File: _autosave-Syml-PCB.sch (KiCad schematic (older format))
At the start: 13 parts

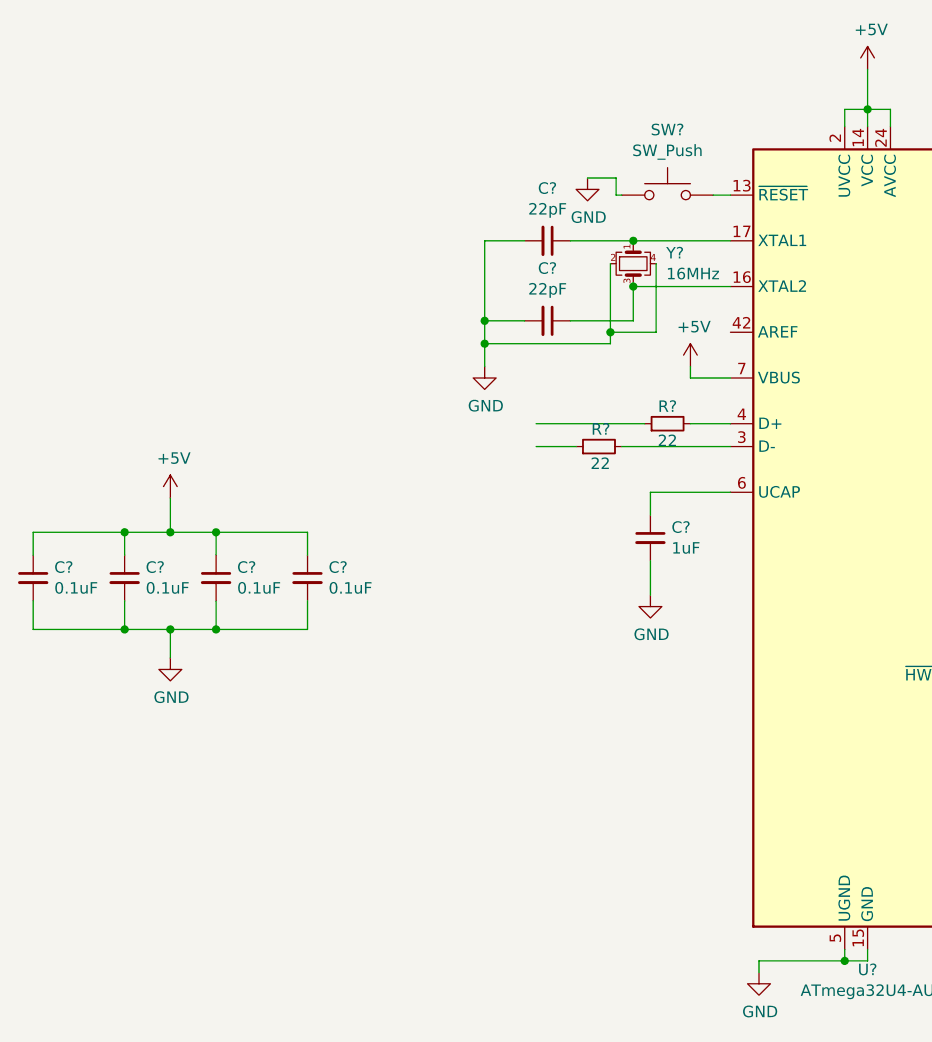
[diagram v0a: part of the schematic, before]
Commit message: Add submodules
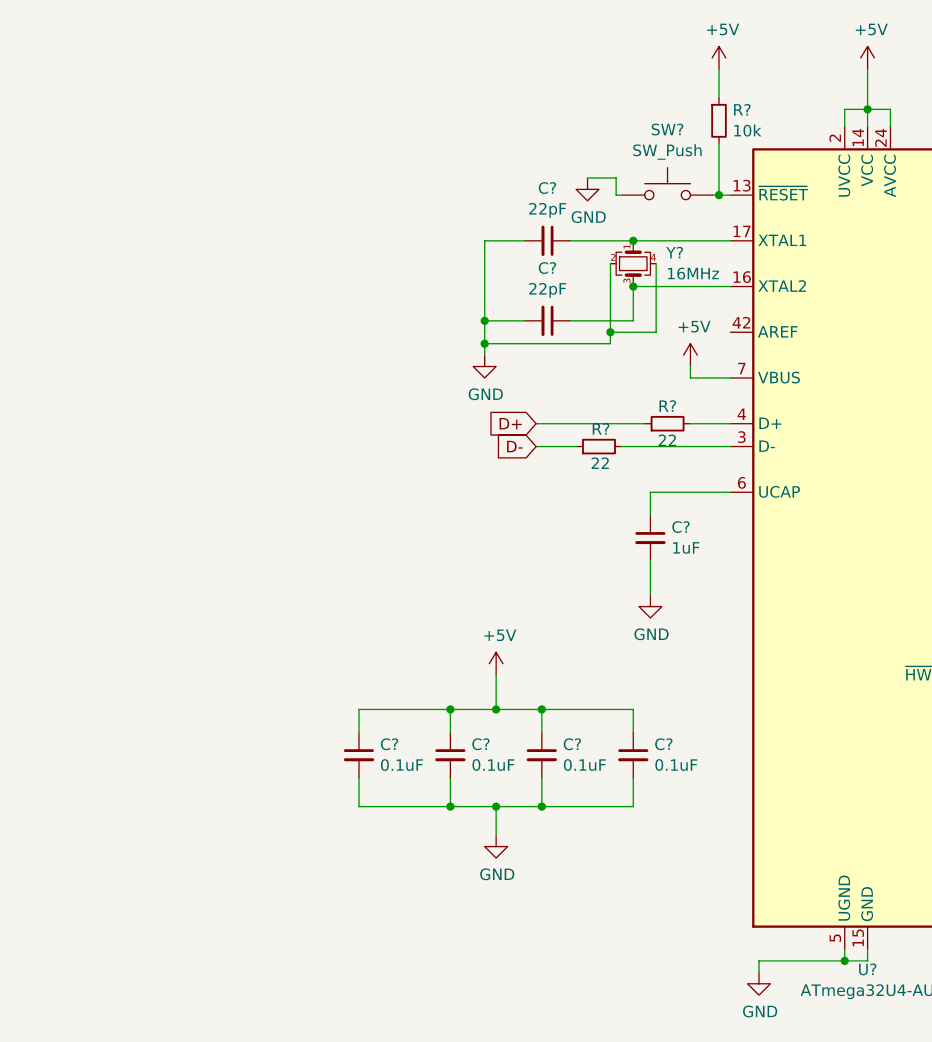
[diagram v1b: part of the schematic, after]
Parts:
- added R?: 10k, symbol Device:R_Small
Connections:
- net labels added: D+, D-
- wire segments 60 -> 63
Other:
- moved on the sheet: C?
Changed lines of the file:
@@
 L Device:C_Small C?
 U 1 1 5CD09A3C
-P 2350 4575
-F 0 "C?" H 2442 4621 50  0000 L CNN
-F 1 "0.1uF" H 2442 4530 50  0000 L CNN
-F 2 "" H 2350 4575 50  0001 C CNN
-F 3 "~" H 2350 4575 50  0001 C CNN
-	1    2350 4575
+P 3775 5350
+F 0 "C?" H 3867 5396 50  0000 L CNN
+F 1 "0.1uF" H 3867 5305 50  0000 L CNN
+F 2 "" H 3775 5350 50  0001 C CNN
+F 3 "~" H 3775 5350 50  0001 C CNN
+	1    3775 5350
 	1    0    0    -1
 $EndComp
@@
 L Device:C_Small C?
 U 1 1 5CD0A82B
-P 2750 4575
-F 0 "C?" H 2842 4621 50  0000 L CNN
-F 1 "0.1uF" H 2842 4530 50  0000 L CNN
-F 2 "" H 2750 4575 50  0001 C CNN
-F 3 "~" H 2750 4575 50  0001 C CNN
-	1    2750 4575
+P 4175 5350
+F 0 "C?" H 4267 5396 50  0000 L CNN
+F 1 "0.1uF" H 4267 5305 50  0000 L CNN
+F 2 "" H 4175 5350 50  0001 C CNN
+F 3 "~" H 4175 5350 50  0001 C CNN
+	1    4175 5350
 	1    0    0    -1
 $EndComp
@@
 L Device:C_Small C?
 U 1 1 5CD0AD4B
-P 1950 4575
-F 0 "C?" H 2042 4621 50  0000 L CNN
-F 1 "0.1uF" H 2042 4530 50  0000 L CNN
-F 2 "" H 1950 4575 50  0001 C CNN
-F 3 "~" H 1950 4575 50  0001 C CNN
-	1    1950 4575
+P 3375 5350
+F 0 "C?" H 3467 5396 50  0000 L CNN
+F 1 "0.1uF" H 3467 5305 50  0000 L CNN
+F 2 "" H 3375 5350 50  0001 C CNN
+F 3 "~" H 3375 5350 50  0001 C CNN
+	1    3375 5350
 	1    0    0    -1
 $EndComp
@@
 L Device:C_Small C?
 U 1 1 5CD0B432
-P 1550 4575
-F 0 "C?" H 1642 4621 50  0000 L CNN
-F 1 "0.1uF" H 1642 4530 50  0000 L CNN
-F 2 "" H 1550 4575 50  0001 C CNN
-F 3 "~" H 1550 4575 50  0001 C CNN
-	1    1550 4575
-	1    0    0    -1
-$EndComp
-Wire Wire Line
-	1550 4475 1550 4375
-Wire Wire Line
-	1550 4375 1950 4375
-Wire Wire Line
-	2750 4375 2750 4475
-Wire Wire Line
-	1550 4675 1550 4800
-Wire Wire Line
-	1550 4800 1950 4800
-Wire Wire Line
-	2750 4800 2750 4675
-Wire Wire Line
-	1950 4475 1950 4375
-Connection ~ 1950 4375
-Wire Wire Line
-	1950 4375 2150 4375
-Wire Wire Line
-	2350 4475 2350 4375
-Connection ~ 2350 4375
-Wire Wire Line
-	2350 4375 2750 4375
-Wire Wire Line
-	1950 4675 1950 4800
-Connection ~ 1950 4800
-Wire Wire Line
-	1950 4800 2150 4800
-Wire Wire Line
-	2350 4675 2350 4800
-Connection ~ 2350 4800
-Wire Wire Line
-	2350 4800 2750 4800
+P 2975 5350
+F 0 "C?" H 3067 5396 50  0000 L CNN
+F 1 "0.1uF" H 3067 5305 50  0000 L CNN
+F 2 "" H 2975 5350 50  0001 C CNN
+F 3 "~" H 2975 5350 50  0001 C CNN
+	1    2975 5350
+	1    0    0    -1
+$EndComp
+Wire Wire Line
+	2975 5250 2975 5150
+Wire Wire Line
+	2975 5150 3375 5150
+Wire Wire Line
+	4175 5150 4175 5250
+Wire Wire Line
+	2975 5450 2975 5575
+Wire Wire Line
+	2975 5575 3375 5575
+Wire Wire Line
+	4175 5575 4175 5450
+Wire Wire Line
+	3375 5250 3375 5150
+Connection ~ 3375 5150
+Wire Wire Line
+	3375 5150 3575 5150
+Wire Wire Line
+	3775 5250 3775 5150
+Connection ~ 3775 5150
+Wire Wire Line
+	3775 5150 4175 5150
+Wire Wire Line
+	3375 5450 3375 5575
+Connection ~ 3375 5575
+Wire Wire Line
+	3375 5575 3575 5575
+Wire Wire Line
+	3775 5450 3775 5575
+Connection ~ 3775 5575
+Wire Wire Line
+	3775 5575 4175 5575
 $Comp
 L power:GND #PWR?
 U 1 1 5CD0FBB1
-P 2150 4925
-F 0 "#PWR?" H 2150 4675 50  0001 C CNN
-F 1 "GND" H 2155 4752 50  0000 C CNN
-F 2 "" H 2150 4925 50  0001 C CNN
-F 3 "" H 2150 4925 50  0001 C CNN
-	1    2150 4925
+P 3575 5700
+F 0 "#PWR?" H 3575 5450 50  0001 C CNN
+F 1 "GND" H 3580 5527 50  0000 C CNN
+F 2 "" H 3575 5700 50  0001 C CNN
+F 3 "" H 3575 5700 50  0001 C CNN
+	1    3575 5700
 	1    0    0    -1
 $EndComp
@@
 L power:+5V #PWR?
 U 1 1 5CD10337
-P 2150 4225
-F 0 "#PWR?" H 2150 4075 50  0001 C CNN
-F 1 "+5V" H 2165 4398 50  0000 C CNN
-F 2 "" H 2150 4225 50  0001 C CNN
-F 3 "" H 2150 4225 50  0001 C CNN
-	1    2150 4225
-	1    0    0    -1
-$EndComp
-Wire Wire Line
-	2150 4225 2150 4375
-Connection ~ 2150 4375
-Wire Wire Line
-	2150 4375 2350 4375
-Wire Wire Line
-	2150 4925 2150 4800
-Connection ~ 2150 4800
-Wire Wire Line
-	2150 4800 2350 4800
+P 3575 5000
+F 0 "#PWR?" H 3575 4850 50  0001 C CNN
+F 1 "+5V" H 3590 5173 50  0000 C CNN
+F 2 "" H 3575 5000 50  0001 C CNN
+F 3 "" H 3575 5000 50  0001 C CNN
+	1    3575 5000
+	1    0    0    -1
+$EndComp
+Wire Wire Line
+	3575 5000 3575 5150
+Connection ~ 3575 5150
+Wire Wire Line
+	3575 5150 3775 5150
+Wire Wire Line
+	3575 5700 3575 5575
+Connection ~ 3575 5575
+Wire Wire Line
+	3575 5575 3775 5575
 $Comp
 L power:+5V #PWR?
@@
 	0    1    1    0
 $EndComp
-$Comp
-L power:GND #PWR?
-U 1 1 5CD23FFA
-P 3525 3650
-F 0 "#PWR?" H 3525 3400 50  0001 C CNN
-F 1 "GND" H 3530 3477 50  0000 C CNN
-F 2 "" H 3525 3650 50  0001 C CNN
-F 3 "" H 3525 3650 50  0001 C CNN
-	1    3525 3650
-	1    0    0    -1
-$EndComp
 Wire Wire Line
 	4175 3100 3900 3100
@@
 Wire Wire Line
 	4075 3550 3525 3550
-Connection ~ 3525 3550
 Wire Wire Line
 	4275 3200 4275 3500
@@
 Wire Wire Line
 	4425 3700 4425 3650
-Wire Wire Line
-	3525 3550 3525 3650
 $Comp
 L Switch:SW_Push SW?
@@
 $EndComp
 Wire Wire Line
-	4600 2900 4525 2900
+	4600 2900 4550 2900
 Wire Wire Line
 	4125 2900 4100 2900
@@
 Wire Wire Line
 	4100 2825 3975 2825
+$Comp
+L Device:R_Small R?
+U 1 1 5CD3BD7A
+P 4550 2575
+F 0 "R?" H 4609 2621 50  0000 L CNN
+F 1 "10k" H 4609 2530 50  0000 L CNN
+F 2 "" H 4550 2575 50  0001 C CNN
+F 3 "~" H 4550 2575 50  0001 C CNN
+	1    4550 2575
+	1    0    0    -1
+$EndComp
+Wire Wire Line
+	4550 2900 4550 2675
+Connection ~ 4550 2900
+Wire Wire Line
+	4550 2900 4525 2900
+$Comp
+L power:+5V #PWR?
+U 1 1 5CD3DC30
+P 4550 2350
+F 0 "#PWR?" H 4550 2200 50  0001 C CNN
+F 1 "+5V" H 4565 2523 50  0000 C CNN
+F 2 "" H 4550 2350 50  0001 C CNN
+F 3 "" H 4550 2350 50  0001 C CNN
+	1    4550 2350
+	1    0    0    -1
+$EndComp
+Wire Wire Line
+	4550 2475 4550 2350
+Text GLabel 3750 3900 0    50   Input ~ 0
+D+
+$Comp
+L power:GND #PWR?
+U 1 1 5CD23FFA
+P 3525 3600
+F 0 "#PWR?" H 3525 3350 50  0001 C CNN
+F 1 "GND" H 3530 3427 50  0000 C CNN
+F 2 "" H 3525 3600 50  0001 C CNN
+F 3 "" H 3525 3600 50  0001 C CNN
+	1    3525 3600
+	1    0    0    -1
+$EndComp
+Wire Wire Line
+	3525 3550 3525 3600
+Connection ~ 3525 3550
+Text GLabel 3750 4000 0    50   Input ~ 0
+D-
 $EndSCHEMATC

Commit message: Add submodules
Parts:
- added A1, Apostrophe1, B1, BSlash1, Back1, Back2, C1, Comma1, D1, DArrow1, Del1, E1, Enter1, Equal1, Esc1, F0, F1, F10, F11, F12, F2, F3, F4, F5, F6, F7, F8, F9, G1, H1, Home1, I1, J1, K1, L1, LArrow1, LBracket1, LShift2, M1, MX0, MX1, MX2, MX3, MX4, MX5, MX6, MX7, MX8, MX9, Minus1, N1, O1, P1, Period1, PgDn1, PgUp1, Q1, R1, RArrow1, RBracket1, S1, Semicolon1, T1, TArrow1, Tilda1, U1, V1, W1, X1, Y1, Z1: MX-1U, MX_Alps_Hybrid:MX-1U, symbol MX_Alps_Hybrids:MX-1U
- added CLF1: 1800mA, Fuse:Fuse_1206_3216Metric, symbol Device:Polyfuse_Small
- added CapsLock1, RShift1: MX-1U, MX_Alps_Hybrid:MX-1.75U, symbol MX_Alps_Hybrids:MX-1U
- added D10, D11, D12, D13, D14, D15, D16, D17, D18, D19, D2, D20, D21, D22, D23, D24, D25, D26, D27, D28, D29, D3, D30, D31, D32, D33, D34, D35, D36, D37, D38, D39, D4, D40, D41, D42, D43, D44, D45, D46, D47, D48, D49, D5, D50, D51, D52, D53, D54, D55, D56, D57, D58, D59, D6, D60, D61, D62, D63, D64, D65, D66, D67, D68, D69, D7, D70, D71, D72, D73, D74, D75, D76, D77, D78, D79, D8, D80, D81, D82, D83, D84, D9: SOD-123, random-keyboard-parts:D_SOD-123-Pretty, symbol Device:D_Small
- added Enter2: MX-1U, MX_Alps_Hybrid:MX-2.25U, symbol MX_Alps_Hybrids:MX-1U
- added FSlash1, RAlt1, RCtrl1, Tab1: MX-1U, MX_Alps_Hybrid:MX-1.5U, symbol MX_Alps_Hybrids:MX-1U
- added LAlt1, LCtrl1, LShift1, LWK1: MX-1U, MX_Alps_Hybrid:MX-1.25U, symbol MX_Alps_Hybrids:MX-1U
- added R4, R6: 5.1k, Resistor_SMD:R_0805_2012Metric, symbol Device:R_Small
- added Space1: MX-1U, MX_Alps_Hybrid:MX-6.25U-ReversedStabilizers, symbol MX_Alps_Hybrids:MX-1U
- added U3, U4: IS31FL3733, Package_QFP:TQFP-48-1EP_7x7mm_P0.5mm_EP5x5mm, symbol random-keyboard-parts:IS31FL3733
- added USB1: 12401598E4#2A, Type-C:12401598E4#2A, symbol Type-C:12401598E4#2A
- C2, C3, C4, C5, C6, C7, C8: renamed from C?; footprint (none) -> Capacitor_SMD:C_0805_2012Metric
- R2, R3, R5, R7: renamed from R?; footprint (none) -> Resistor_SMD:R_0805_2012Metric
- SW1: renamed from SW?; footprint (none) -> random-keyboard-parts:SKQG-1155865
- Y2: renamed from Y?; footprint (none) -> Crystal:Crystal_SMD_3225-4Pin_3.2x2.5mm
- gave numbers to parts that had none: 1
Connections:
- net +5V: now also CLF1.1
- net D+: now also USB1.A6 (D+), USB1.B6 (D+)
- net D-: now also USB1.A7 (D-), USB1.B7 (D-)
- net GND: now also R4.2, R6.2, U3.12 (PGND), U3.34 (AGND), U3.5 (PGND), U4.12 (PGND), U4.34 (AGND), U4.5 (PGND), USB1.A1 (GND), USB1.A12 (GND), USB1.B1 (GND), USB1.B12 (GND), USB1.S1 (Shell1), USB1.S2 (Shell2), USB1.S3 (Shell3), USB1.S4 (Shell4)
- new net: D23.2 (A), Esc1.2 (ROW)
- new net: D7.2 (A), F1.2 (ROW)
- new net: D2.2 (A), Tilda1.2 (ROW)
- new net: D8.2 (A), MX1.2 (ROW)
- new net: D12.2 (A), F2.2 (ROW)
- new net: D18.2 (A), F3.2 (ROW)
- new net: D13.2 (A), MX2.2 (ROW)
- new net: D19.2 (A), MX3.2 (ROW)
- new net: R6.1, USB1.A5 (CC1)
- new net: R4.1, USB1.B5 (CC2)
- new net: D24.2 (A), F4.2 (ROW)
- new net: D29.2 (A), F5.2 (ROW)
- new net: D25.2 (A), MX4.2 (ROW)
- new net: D30.2 (A), MX5.2 (ROW)
- new net: D34.2 (A), F6.2 (ROW)
- new net: D40.2 (A), F7.2 (ROW)
- new net: D35.2 (A), MX6.2 (ROW)
- new net: D41.2 (A), MX7.2 (ROW)
- new net: D45.2 (A), F8.2 (ROW)
- new net: D50.2 (A), F9.2 (ROW)
- new net: D46.2 (A), MX8.2 (ROW)
- new net: D51.2 (A), MX9.2 (ROW)
- new net: D55.2 (A), F10.2 (ROW)
- new net: D61.2 (A), F11.2 (ROW)
- new net: D56.2 (A), MX0.2 (ROW)
- new net: D62.2 (A), Minus1.2 (ROW)
- new net: D67.2 (A), F12.2 (ROW)
- new net: D68.2 (A), Equal1.2 (ROW)
- new net: Back1.2 (ROW), D71.2 (A)
- new net: D79.2 (A), Del1.2 (ROW)
- new net: Back2.2 (ROW), D76.2 (A)
- new net: D80.2 (A), Home1.2 (ROW)
- new net: D3.2 (A), Tab1.2 (ROW)
- new net: D9.2 (A), Q1.2 (ROW)
- new net: CapsLock1.2 (ROW), D4.2 (A)
- new net: A1.2 (ROW), D10.2 (A)
- new net: D14.2 (A), W1.2 (ROW)
- new net: D20.2 (A), E1.2 (ROW)
- new net: D15.2 (A), S1.2 (ROW)
- new net: D1.2 (ROW), D21.2 (A)
- new net: D26.2 (A), R1.2 (ROW)
- new net: D31.2 (A), T1.2 (ROW)
- new net: D27.2 (A), F0.2 (ROW)
- new net: D32.2 (A), G1.2 (ROW)
- new net: D36.2 (A), Y1.2 (ROW)
- new net: D42.2 (A), U1.2 (ROW)
- new net: D37.2 (A), H1.2 (ROW)
- new net: D43.2 (A), J1.2 (ROW)
- new net: D47.2 (A), I1.2 (ROW)
- new net: D52.2 (A), O1.2 (ROW)
- new net: D48.2 (A), K1.2 (ROW)
- new net: D53.2 (A), L1.2 (ROW)
- new net: D57.2 (A), P1.2 (ROW)
- new net: D63.2 (A), LBracket1.2 (ROW)
- new net: D58.2 (A), Semicolon1.2 (ROW)
- new net: Apostrophe1.2 (ROW), D64.2 (A)
- new net: D69.2 (A), RBracket1.2 (ROW)
- new net: D72.2 (A), FSlash1.2 (ROW)
- new net: D70.2 (A), Enter1.2 (ROW)
- new net: D73.2 (A), Enter2.2 (ROW)
- new net: D81.2 (A), PgUp1.2 (ROW)
- new net: D82.2 (A), PgDn1.2 (ROW)
- new net: D5.2 (A), LShift1.2 (ROW)
- new net: D6.2 (A), LCtrl1.2 (ROW)
- new net: D11.2 (A), LWK1.2 (ROW)
- new net: D16.2 (A), Z1.2 (ROW)
- new net: D22.2 (A), X1.2 (ROW)
- new net: D17.2 (A), LAlt1.2 (ROW)
- new net: C1.2 (ROW), D28.2 (A)
- new net: D33.2 (A), V1.2 (ROW)
- new net: B1.2 (ROW), D38.2 (A)
- new net: D44.2 (A), N1.2 (ROW)
- new net: D39.2 (A), Space1.2 (ROW)
- new net: D49.2 (A), M1.2 (ROW)
- new net: Comma1.2 (ROW), D54.2 (A)
- new net: D59.2 (A), Period1.2 (ROW)
- new net: BSlash1.2 (ROW), D65.2 (A)
- new net: D60.2 (A), RAlt1.2 (ROW)
- new net: D66.2 (A), RCtrl1.2 (ROW)
- new net: D74.2 (A), RShift1.2 (ROW)
- new net: D75.2 (A), LArrow1.2 (ROW)
- new net: D77.2 (A), TArrow1.2 (ROW)
- new net: D78.2 (A), DArrow1.2 (ROW)
- new net: D83.2 (A), RArrow1.2 (ROW)
- new net: D84.2 (A), LShift2.2 (ROW)
- new net COL0: CapsLock1.1 (COL), Esc1.1 (COL), LCtrl1.1 (COL), LShift1.1 (COL), Tab1.1 (COL), Tilda1.1 (COL)
- new net COL1: A1.1 (COL), F1.1 (COL), LShift2.1 (COL), LWK1.1 (COL), MX1.1 (COL), Q1.1 (COL)
- new net COL10: F10.1 (COL), MX0.1 (COL), P1.1 (COL), Period1.1 (COL), RAlt1.1 (COL), Semicolon1.1 (COL)
- new net COL11: Apostrophe1.1 (COL), BSlash1.1 (COL), F11.1 (COL), LBracket1.1 (COL), Minus1.1 (COL), RCtrl1.1 (COL)
- new net COL12: Enter1.1 (COL), Equal1.1 (COL), F12.1 (COL), RBracket1.1 (COL)
- new net COL13: Back1.1 (COL), Enter2.1 (COL), FSlash1.1 (COL), LArrow1.1 (COL), RShift1.1 (COL)
- new net COL14: Back2.1 (COL), DArrow1.1 (COL), TArrow1.1 (COL)
- new net COL15: Del1.1 (COL), Home1.1 (COL), PgDn1.1 (COL), PgUp1.1 (COL), RArrow1.1 (COL)
- new net COL2: F2.1 (COL), LAlt1.1 (COL), MX2.1 (COL), S1.1 (COL), W1.1 (COL), Z1.1 (COL)
- new net COL3: D1.1 (COL), E1.1 (COL), F3.1 (COL), MX3.1 (COL), X1.1 (COL)
- new net COL4: C1.1 (COL), F0.1 (COL), F4.1 (COL), MX4.1 (COL), R1.1 (COL)
- new net COL5: F5.1 (COL), G1.1 (COL), MX5.1 (COL), T1.1 (COL), V1.1 (COL)
- new net COL6: B1.1 (COL), F6.1 (COL), H1.1 (COL), MX6.1 (COL), Space1.1 (COL), Y1.1 (COL)
- new net COL7: F7.1 (COL), J1.1 (COL), MX7.1 (COL), N1.1 (COL), U1.1 (COL)
- new net COL8: F8.1 (COL), I1.1 (COL), K1.1 (COL), M1.1 (COL), MX8.1 (COL)
- new net COL9: Comma1.1 (COL), F9.1 (COL), L1.1 (COL), MX9.1 (COL), O1.1 (COL)
- new net ROW0: D12.1 (K), D18.1 (K), D23.1 (K), D24.1 (K), D29.1 (K), D34.1 (K), D40.1 (K), D45.1 (K), D50.1 (K), D55.1 (K), D61.1 (K), D67.1 (K), D7.1 (K), D79.1 (K)
- new net ROW1: D13.1 (K), D19.1 (K), D2.1 (K), D25.1 (K), D30.1 (K), D35.1 (K), D41.1 (K), D46.1 (K), D51.1 (K), D56.1 (K), D62.1 (K), D68.1 (K), D71.1 (K), D76.1 (K), D8.1 (K), D80.1 (K)
- new net ROW2: D14.1 (K), D20.1 (K), D26.1 (K), D3.1 (K), D31.1 (K), D36.1 (K), D42.1 (K), D47.1 (K), D52.1 (K), D57.1 (K), D63.1 (K), D69.1 (K), D72.1 (K), D81.1 (K), D9.1 (K)
- new net ROW3: D10.1 (K), D15.1 (K), D21.1 (K), D27.1 (K), D32.1 (K), D37.1 (K), D4.1 (K), D43.1 (K), D48.1 (K), D53.1 (K), D58.1 (K), D64.1 (K), D70.1 (K), D73.1 (K), D82.1 (K)
- new net ROW4: D16.1 (K), D22.1 (K), D28.1 (K), D33.1 (K), D38.1 (K), D44.1 (K), D49.1 (K), D5.1 (K), D54.1 (K), D59.1 (K), D65.1 (K), D74.1 (K), D77.1 (K), D84.1 (K)
- new net ROW5: D11.1 (K), D17.1 (K), D39.1 (K), D6.1 (K), D60.1 (K), D66.1 (K), D75.1 (K), D78.1 (K), D83.1 (K)
- new net VCC: CLF1.2, USB1.A4 (VBUS), USB1.A9 (VBUS), USB1.B4 (VBUS), USB1.B9 (VBUS)
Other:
- moved on the sheet: C2, C3, C4, C5, C6, C7, C8, R2, R3, R5, R7, SW1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
